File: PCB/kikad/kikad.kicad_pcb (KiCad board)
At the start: 2 copper layers, 228.6 x 137.2 mm, 603 parts, among them M1 SSOP-24_5.3x8.2mm_P0.65mm, M2 SSOP-24_5.3x8.2mm_P0.65mm, m1 PinHeader_1x02_P1.00mm_Vertic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, m2 PinHeader_1x02_P1.00mm_Vertic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, m3 PinHeader_1x02_P1.00mm_Vertic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, m4 PinHeader_1x02_P1.00mm_Vertic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

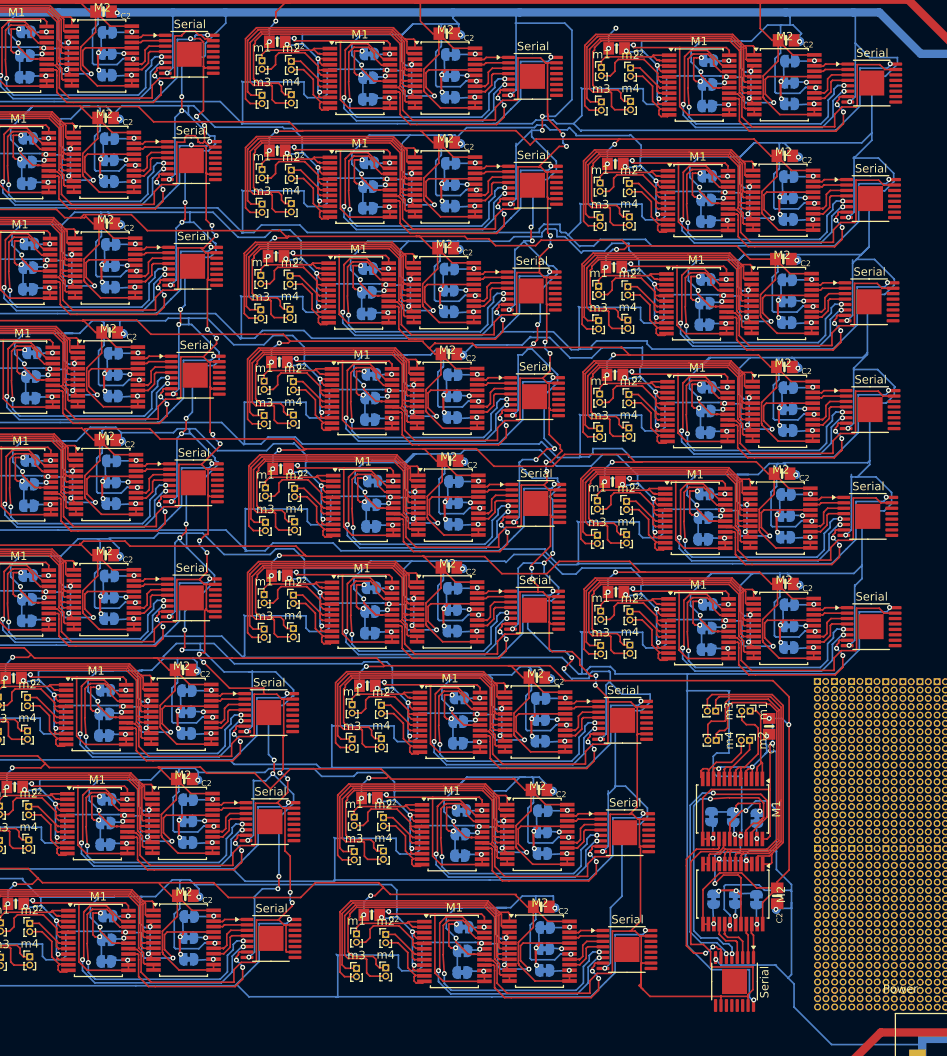
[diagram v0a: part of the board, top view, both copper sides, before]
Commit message: PCB power on serial
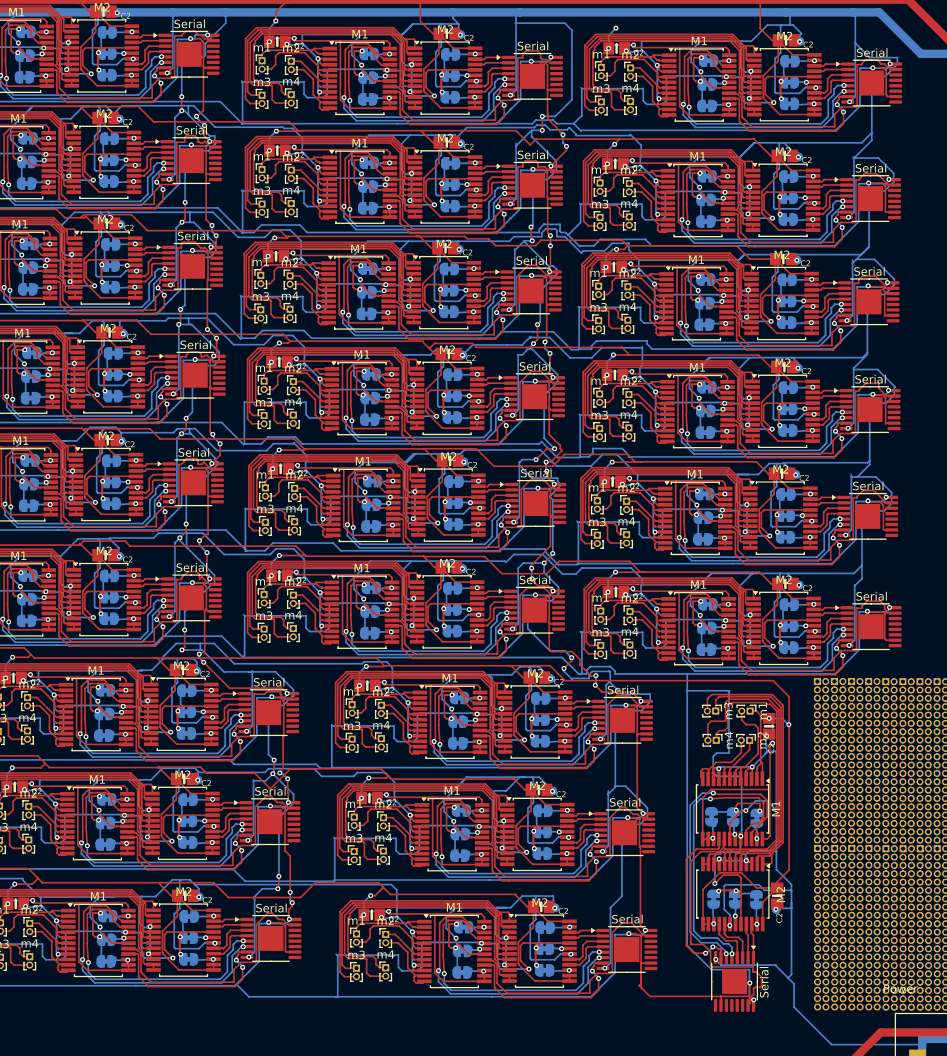
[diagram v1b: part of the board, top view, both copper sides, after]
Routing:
- net (no net): track 19995.4 -> 20083.6 mm, vias 842 -> 865

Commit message: pcb
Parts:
- added big_cap: CP_Radial_D8.0mm_P3.80mm, Capacitor_THT:CP_Radial_D8.0mm_P3.80mm, F.Cu at (221.0, 156.1)
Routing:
- net (no net): track 20083.6 -> 20098.8 mm
